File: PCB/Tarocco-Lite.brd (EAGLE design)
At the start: 47 x 26.3 mm, 37 parts, among them IC1 CY8C4545PVI, U1 DRV8801PWP

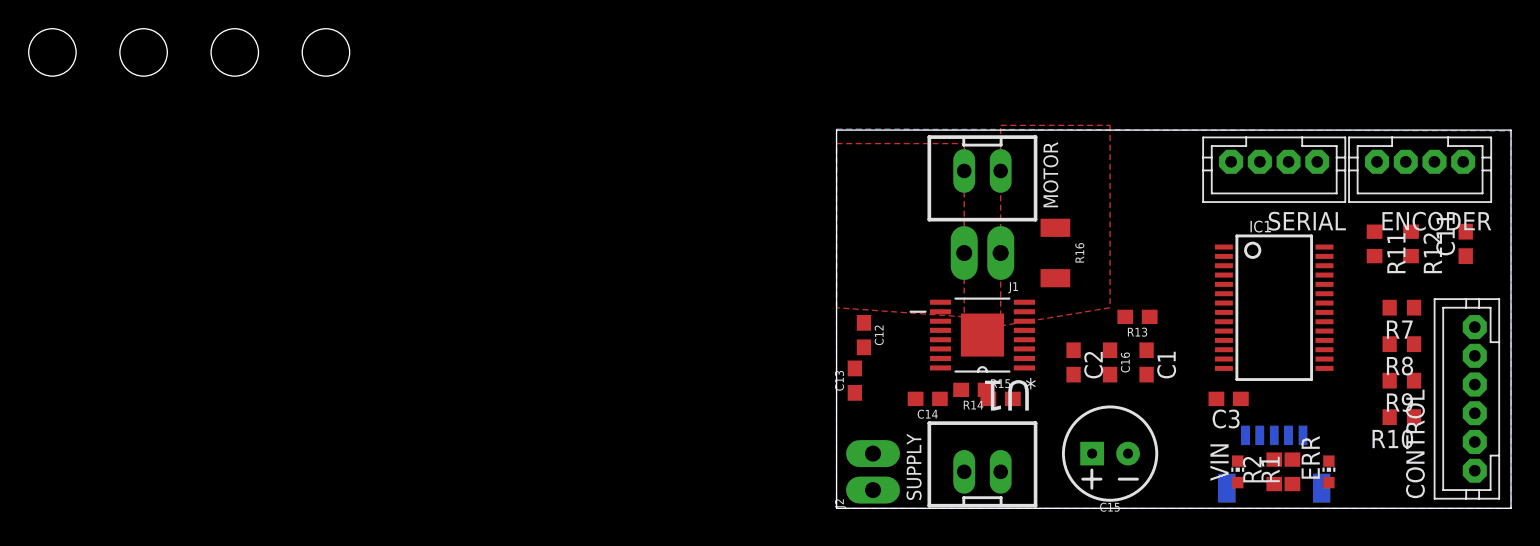
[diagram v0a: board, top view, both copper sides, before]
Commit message: Rename and mostly routed
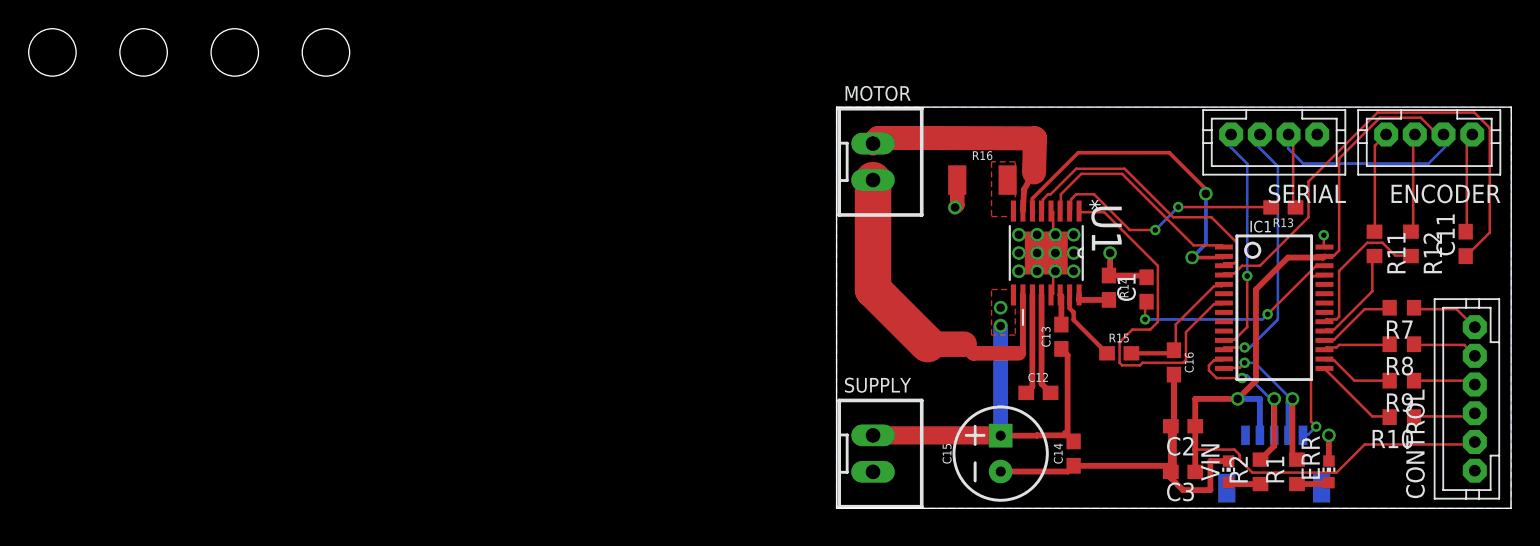
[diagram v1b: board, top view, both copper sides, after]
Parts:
- removed J1, J2: (no value), SparkFun-Connectors:1X02_LONGPADS
- moved C13 14.7 mm to (25.8, 11.9)
- moved C12 12.8 mm to (24.2, 8.04), turned to 0 degrees
- moved R13 12.7 mm to (41.3, 21.0)
- moved R14 11.8 mm to (29.1, 15.4), turned to 270 degrees
- moved C14 10.9 mm to (26.7, 3.81), turned to 90 degrees
- moved R15 8.84 mm to (29.8, 10.8)
- moved C2 8.82 mm to (34.3, 5.71), turned to 180 degrees
- moved SUPPLY 7.73 mm to (12.7, 3.81), turned to 270 degrees
- moved MOTOR 7.65 mm to (12.7, 24.1), turned to 270 degrees
- moved C15 7.62 mm to (21.6, 3.81), turned to 90 degrees
- moved U1 7.24 mm to (24.8, 17.8), turned to 270 degrees
- moved R16 7.18 mm to (20.3, 22.9), turned to 0 degrees
- moved C3 5.99 mm to (34.3, 2.54)
- moved C1 5.08 mm to (31.8, 15.2), turned to 90 degrees
- moved C16 4.45 mm to (33.7, 10.2)
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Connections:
- net N$36 renamed SENSE
- removed net N$26: C13.1, C14.2, C15.1, J2.1, SUPPLY.1, U1.9
- new net VBB: C13.1, C14.2, C15.1, SUPPLY.1, U1.9
- net GND: no longer J2.2
- net VMOT+: no longer J1.1
- net VMOT-: no longer J1.2
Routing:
- net 5V: track 0.00 -> 83.2 mm, vias 0 -> 1
- net GND: track 0.00 -> 52.3 mm, vias 0 -> 16
- net N$29: track 0.00 -> 34.8 mm
- net VBB: track 0.00 -> 28.3 mm, vias 0 -> 2
- net FAULT: track 0.00 -> 25.9 mm
- net VMOT-: track 0.00 -> 23.8 mm
- net ENABLE: track 0.00 -> 22.7 mm, vias 0 -> 2
- net SLEEP: track 0.00 -> 19.8 mm
- net TXD: track 0.00 -> 18.3 mm, vias 0 -> 1
- net VMOT+: track 0.00 -> 16.7 mm
- net N$9: track 0.00 -> 16.6 mm, vias 0 -> 2
- net RXD: track 0.00 -> 16.0 mm, vias 0 -> 1
- net N$19: track 0.00 -> 15.3 mm, vias 0 -> 2
- net PHASE: track 0.00 -> 15.2 mm
- net SWDIO: track 0.00 -> 14.4 mm, vias 0 -> 2
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- added copper zone on layer 1, net SENSE
- added copper zone on layer 1, net VBB
- removed copper zone on layer 1, net VMOT+
- removed copper zone on layer 1, net VMOT-
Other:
- board size 47 x 26.3 mm -> 47 x 27.9 mm

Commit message: Alpha finished
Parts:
- removed STANDOFF1, STANDOFF2, STANDOFF3, STANDOFF4: STAND-OFF, SparkFun-Electromechanical:STAND-OFF
- moved C1 15.7 mm to (47.3, 17.1)
- moved R12 2.56 mm to (52.4, 17.1)
- moved R11 2.56 mm to (49.8, 17.1)
- moved R7 2.13 mm to (47.6, 13.0)
- moved R8 2.01 mm to (47.6, 10.8)
- moved R9 1.93 mm to (47.6, 8.57)
- moved R10 1.91 mm to (47.6, 6.35)
- moved C11 1.59 mm to (54.9, 17.1)
- moved CONTROL 0.32 mm to (54.6, 7.30)
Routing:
- net 5V: track 83.2 -> 70.3 mm
- net N$19: track 15.3 -> 3.44 mm, vias 2 -> 0
- net N$29: track 34.8 -> 45.3 mm
- net GND: track 52.3 -> 61.5 mm, vias 16 -> 15
- net DIRECTION: track 5.46 -> 3.18 mm
- net STEP: track 4.70 -> 2.75 mm
- net N$10: track 6.91 -> 8.84 mm
- net N$22: track 4.34 -> 6.23 mm
- net N$20: track 4.37 -> 6.25 mm
- net N$18: track 4.56 -> 6.36 mm
- net RESET: track 5.15 -> 3.45 mm
- net N$14: track 4.78 -> 6.49 mm
- net N$8: track 7.10 -> 8.62 mm
- net ERROR: track 5.94 -> 4.48 mm
- net ENABLE: track 22.7 -> 22.0 mm
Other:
- board size 47 x 27.9 mm -> 46.4 x 27.9 mm
- board text added: "+"
- board text added: "+8-36V"
- board text added: "CONTROL"
- board text added: "MOTOR"

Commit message: Added Image
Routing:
- net GND: vias 15 -> 27
- added copper zone on layer 1, net GND
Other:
- board text added: "M^6 Designs"
- board text added: "Tarocco-Lite"
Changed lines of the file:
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@@
 <text x="10.795" y="19.3675" size="1.016" layer="25" align="center-left">MOTOR</text>
 <text x="50.8" y="3.4925" size="1.4224" layer="25" rot="R90" align="center-left">CONTROL</text>
-<text x="16.8275" y="5.08" size="1.6764" layer="25" align="center-left">+</text>
-<text x="16.51" y="25.7175" size="2.1844" layer="25" align="center-left">+</text>
+<text x="16.51" y="5.08" size="2.54" layer="25" align="center-left">+</text>
+<text x="16.51" y="25.7175" size="2.54" layer="25" align="center-left">+</text>
+<text x="24.765" y="0.9525" size="1.016" layer="25" align="center-left">M^6 Designs</text>
+<text x="11.7475" y="10.795" size="1.016" layer="25" ratio="16" align="center-left">Tarocco-Lite</text>
 </plain>
 <attributes>
@@
 <wire x1="44.0944" y1="18.3134" x2="44.14" y2="18.195" width="0.1778" layer="1"/>
 <wire x1="43.7388" y1="25.9588" x2="43.64" y2="26.035" width="0.1778" layer="1"/>
+<polygon width="0.254" layer="1">
+<vertex x="27.94" y="19.3675"/>
+<vertex x="27.94" y="16.1925"/>
+<vertex x="20.0025" y="16.1925"/>
+<vertex x="20.0025" y="12.7"/>
+<vertex x="18.0975" y="12.7"/>
+<vertex x="14.9225" y="15.875"/>
+<vertex x="14.9225" y="19.3675"/>
+</polygon>
+<via x="15.5575" y="18.7325" extent="1-16" drill="0.6"/>
+<via x="15.5575" y="16.1925" extent="1-16" drill="0.6"/>
+<via x="18.415" y="13.335" extent="1-16" drill="0.6"/>
+<via x="19.05" y="16.1925" extent="1-16" drill="0.6"/>
+<via x="19.05" y="14.9225" extent="1-16" drill="0.6"/>
+<via x="17.4625" y="14.9225" extent="1-16" drill="0.6"/>
+<via x="17.145" y="16.1925" extent="1-16" drill="0.6"/>
+<via x="15.5575" y="17.4625" extent="1-16" drill="0.6"/>
+<via x="17.145" y="17.4625" extent="1-16" drill="0.6"/>
+<via x="19.05" y="17.4625" extent="1-16" drill="0.6"/>
+<wire x1="20.6375" y1="17.78" x2="20.6375" y2="17.78" width="0" layer="19" extent="1-16"/>
+<via x="19.05" y="18.7325" extent="1-16" drill="0.6"/>
+<via x="17.145" y="18.7325" extent="1-16" drill="0.6"/>
+<wire x1="20.6375" y1="16.8275" x2="20.6375" y2="16.8275" width="0" layer="19" extent="1-16"/>
+<wire x1="20.6375" y1="18.7325" x2="20.6375" y2="18.7325" width="0" layer="19" extent="1-16"/>
 </signal>
 <signal name="5V">

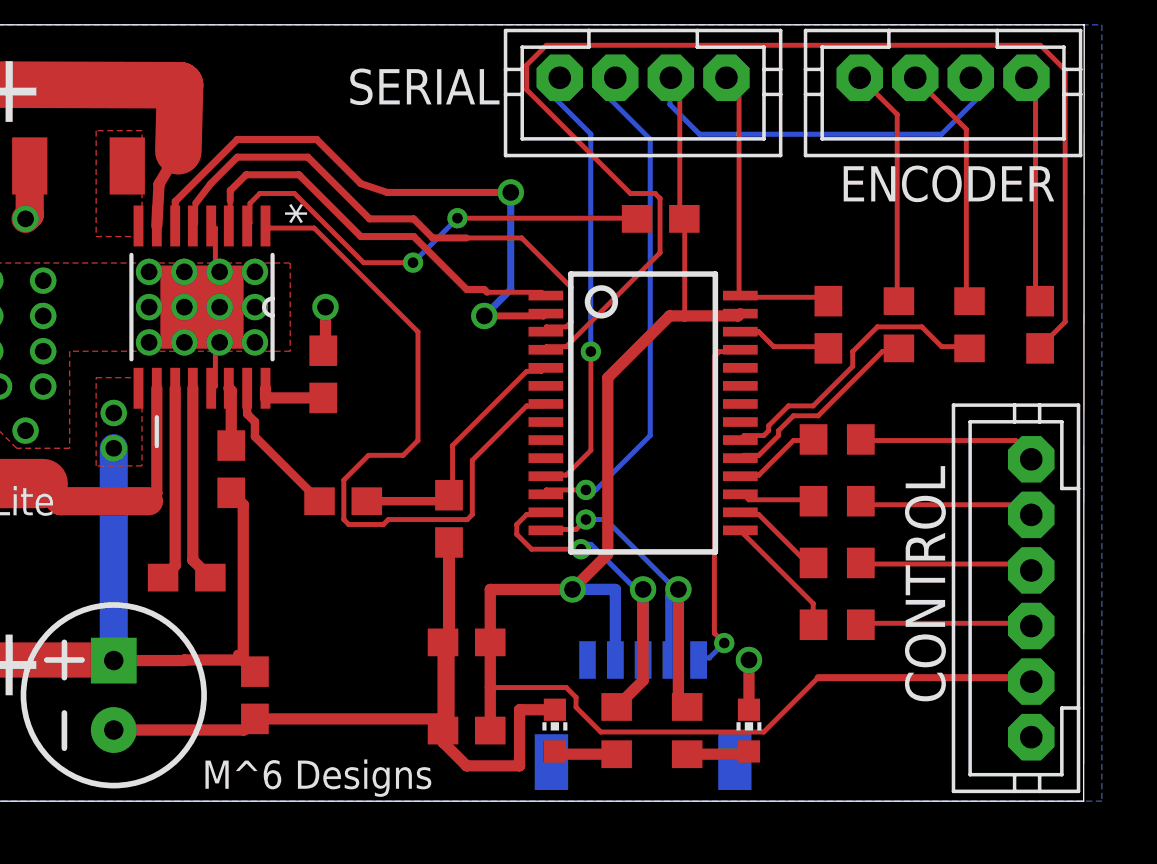
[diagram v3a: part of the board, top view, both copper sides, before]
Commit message: BOM and labelling update
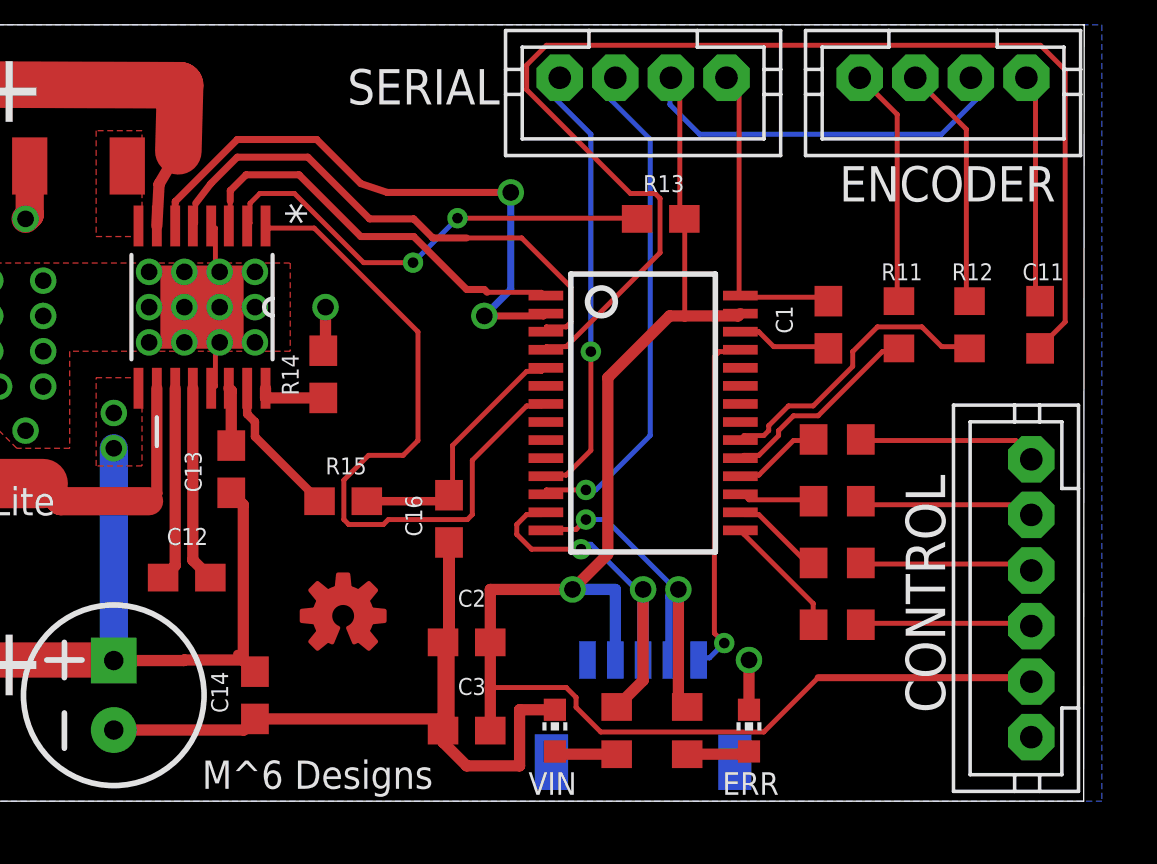
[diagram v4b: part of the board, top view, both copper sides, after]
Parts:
- added U$1: (no value), SparkFun-Aesthetics:OSHW-LOGO-S_COPPER
- R16: value 0.1 -> 0.2
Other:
- board text added: "C1"
- board text added: "C11"
- board text added: "C12"
- board text added: "C13"
- board text added: "C14"
- board text added: "C16"
- board text added: "C2"
- board text added: "C3"
- board text added: "ERR"
- board text added: "GND"
- board text added: "R11"
- board text added: "R12"
- board text added: "R13"
- board text added: "R14"
- board text added: "R15"
- board text added: "VIN"
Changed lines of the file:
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@@
 <text x="10.4775" y="8.5725" size="1.016" layer="25" rot="R180" align="center-right">+8-36V</text>
 <text x="10.795" y="19.3675" size="1.016" layer="25" align="center-left">MOTOR</text>
-<text x="50.8" y="3.4925" size="1.4224" layer="25" rot="R90" align="center-left">CONTROL</text>
+<text x="50.8" y="3.175" size="1.4224" layer="25" rot="R90" align="center-left">CONTROL</text>
 <text x="16.51" y="5.08" size="2.54" layer="25" align="center-left">+</text>
 <text x="16.51" y="25.7175" size="2.54" layer="25" align="center-left">+</text>
 <text x="24.765" y="0.9525" size="1.016" layer="25" align="center-left">M^6 Designs</text>
 <text x="11.7475" y="10.795" size="1.016" layer="25" ratio="16" align="center-left">Tarocco-Lite</text>
+<text x="23.495" y="9.525" size="0.6096" layer="25" align="center-left">C12</text>
+<text x="24.4475" y="11.1125" size="0.6096" layer="25" rot="R90" align="center-left">C13</text>
+<text x="29.21" y="12.065" size="0.6096" layer="25" align="center-left">R15</text>
+<text x="27.94" y="14.605" size="0.6096" layer="25" rot="R90" align="center-left">R14</text>
+<text x="32.385" y="9.525" size="0.6096" layer="25" rot="R90" align="center-left">C16</text>
+<text x="25.4" y="3.175" size="0.6096" layer="25" rot="R90" align="center-left">C14</text>
+<text x="45.72" y="16.8275" size="0.6096" layer="25" rot="R90" align="center-left">C1</text>
+<text x="49.2125" y="19.05" size="0.6096" layer="25" align="center-left">R11</text>
+<text x="51.7525" y="19.05" size="0.6096" layer="25" align="center-left">R12</text>
+<text x="54.2925" y="19.05" size="0.6096" layer="25" align="center-left">C11</text>
+<text x="40.64" y="22.225" size="0.6096" layer="25" align="center-left">R13</text>
+<text x="33.9725" y="7.3025" size="0.6096" layer="25" align="center-left">C2</text>
+<text x="33.9725" y="4.1275" size="0.6096" layer="25" align="center-left">C3</text>
+<text x="36.5125" y="0.635" size="0.8128" layer="25" align="center-left">VIN</text>
+<text x="43.4975" y="0.635" size="0.8128" layer="25" align="center-left">ERR</text>
+<text x="37.7825" y="5.08" size="0.4064" layer="26" rot="MR270" align="center-right">GND</text>
 </plain>
 <attributes>
@@
 <attribute name="PROD_ID" value="RES-07828" x="29.845" y="10.795" size="1.778" layer="27" display="off"/>
 </element>
-<element name="R16" library="SparkFun-Resistors" package="1210" value="0.1" x="20.32" y="22.86" smashed="yes">
+<element name="R16" library="SparkFun-Resistors" package="1210" value="0.2" x="20.32" y="22.86" smashed="yes">
 <attribute name="PROD_ID" value="RES-12374" x="20.32" y="22.86" size="1.778" layer="27" display="off"/>
 </element>
@@
 <attribute name="VALUE" x="39.37" y="1.905" size="1.27" layer="27" rot="R90"/>
 </element>
+<element name="U$1" library="SparkFun-Aesthetics" package="OSHW-LOGO-S_COPPER" value="" x="29.845" y="6.6675"/>
 </elements>
 <signals>

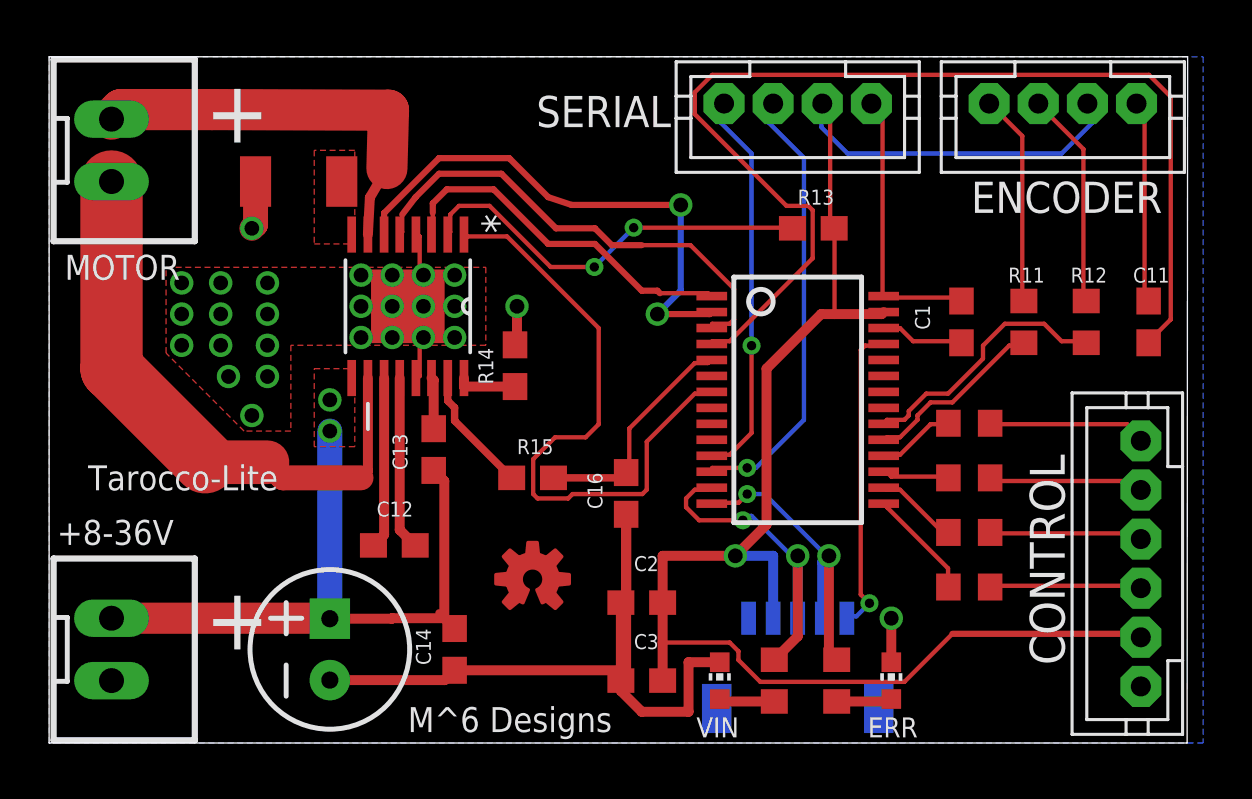
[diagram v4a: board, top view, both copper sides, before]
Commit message: SO MUCH CLEANER
Cleaned up a lot of the layout to reduce crosstalk
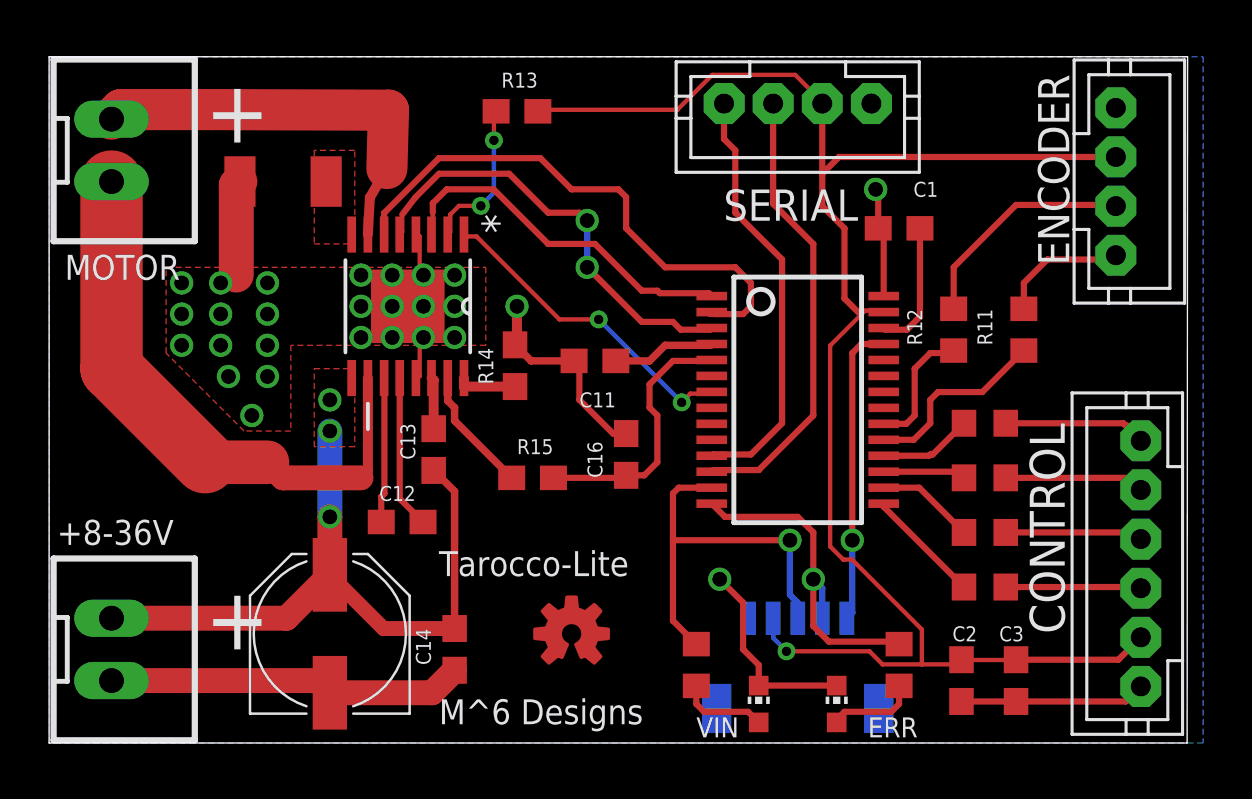
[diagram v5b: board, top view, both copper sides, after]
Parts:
- C15: device SparkFun-Capacitors:CPOL-RADIAL-2.5MM-6.5MM -> SparkFun-Capacitors:PANASONIC_D
- moved C11 22.6 mm to (32.4, 15.6), turned to 180 degrees
- moved C2 15.6 mm to (49.5, 2.54), turned to 270 degrees
- moved C3 13.0 mm to (47.3, 2.54), turned to 270 degrees
- moved R13 13.0 mm to (29.2, 25.7)
- moved R12 5.41 mm to (47.0, 16.8)
- moved C1 4.58 mm to (44.8, 21.0), turned to 180 degrees
- moved ENCODER 3.84 mm to (53.6, 22.9), turned to 270 degrees
- moved R2 3.24 mm to (36.5, 3.17)
- moved U$1 2.73 mm to (31.4, 4.45)
- moved R1 2.62 mm to (44.8, 3.17)
- moved ERR 2.42 mm to (42.2, 1.59)
- moved VIN 1.85 mm to (39.1, 1.59)
- moved C16 1.59 mm to (33.7, 11.7), turned to 90 degrees
- moved C12 1.00 mm to (24.5, 9.00)
- moved R16 0.64 mm to (19.7, 22.9)
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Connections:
- net GND: now also C15.-; no longer C15.2
- net VBB: now also C15.+; no longer C15.1
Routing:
- net N$29: track 45.3 -> 4.19 mm
- net FAULT: track 25.9 -> 13.1 mm, vias 0 -> 2
- net N$9: track 16.6 -> 6.35 mm
- net GND: track 61.5 -> 51.6 mm
- net B: track 10.7 -> 5.20 mm
- net N$8: track 8.62 -> 5.27 mm
- net SLEEP: track 20.1 -> 18.0 mm, vias 0 -> 2
- net SWDIO: track 14.4 -> 16.3 mm, vias 2 -> 1
- net N$19: track 3.44 -> 5.32 mm
- net 5V: track 70.3 -> 68.7 mm
- net RXD: track 16.0 -> 17.4 mm, vias 1 -> 0
- net N$24: track 2.32 -> 3.66 mm
- net ISENSE: track 9.46 -> 10.7 mm
- net N$25: track 2.32 -> 3.59 mm
- net N$28: track 6.99 -> 5.92 mm
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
